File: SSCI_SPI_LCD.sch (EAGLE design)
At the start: 33 parts, among them IC3 74LVC541_RGY, X1 PHA-1X08SG, X2 PHA-1X08SG

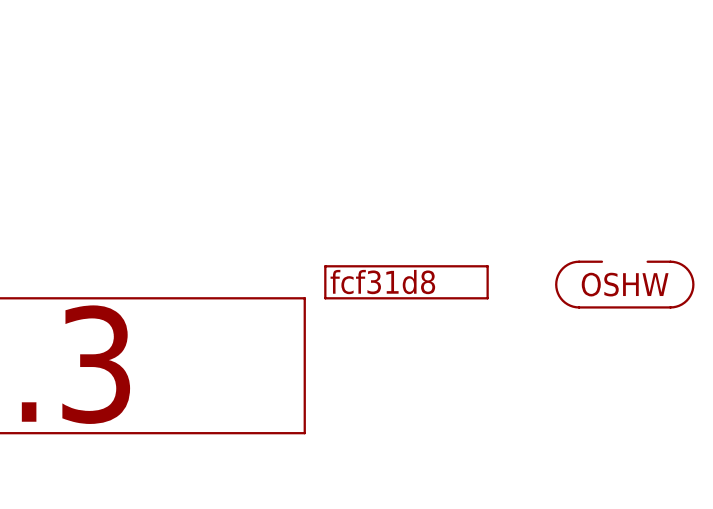
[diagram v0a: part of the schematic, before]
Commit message: update git revision; remove unnecessary tRestrict
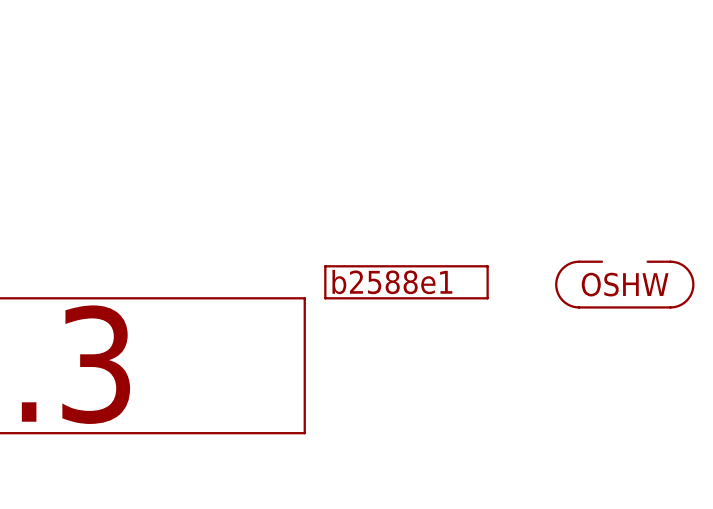
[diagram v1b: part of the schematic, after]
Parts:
- GIT1: value fcf31d8 -> b2588e1
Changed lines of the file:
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@@
 <part name="P3" library="mylib" deviceset="PCB_CORNER" device=""/>
 <part name="P4" library="mylib" deviceset="PCB_CORNER" device=""/>
-<part name="GIT1" library="git-revision" deviceset="GIT-REVISION" device="_1.2" value="fcf31d8"/>
+<part name="GIT1" library="git-revision" deviceset="GIT-REVISION" device="_1.2" value="b2588e1"/>
 <part name="FRAME1" library="frames" deviceset="A4L-LOC" device=""/>
 <part name="ICON1" library="mylib" deviceset="ICON_REVISION" device="_1.7" value="r0.3"/>

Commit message: pin header distance get 200mil narrower
- 1300mil -> 1100mil
- matches with "standard" breadboard
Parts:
- R1: NOT_COMPONENT (none) -> YES
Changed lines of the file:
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@@
 <part name="SUPPLY7" library="mylib" deviceset="GND" device=""/>
 <part name="R2" library="mylib" deviceset="R_US_*" device="_1005" technology="10K"/>
-<part name="R1" library="mylib" deviceset="R_US_*" device="_1005" technology="10K"/>
+<part name="R1" library="mylib" deviceset="R_US_*" device="_1005" technology="10K">
+<attribute name="NOT_COMPONENT" value="YES"/>
+</part>
 <part name="R5" library="mylib" deviceset="R_US_*" device="_1005" technology="10K"/>
 <part name="R3" library="mylib" deviceset="R_US_*" device="_1005" technology="10K"/>
@@
 <instance part="SUPPLY7" gate="GND" x="182.88" y="76.2"/>
 <instance part="R2" gate="G$1" x="83.82" y="160.02"/>
-<instance part="R1" gate="G$1" x="83.82" y="162.56"/>
+<instance part="R1" gate="G$1" x="83.82" y="162.56">
+<attribute name="NOT_COMPONENT" x="83.82" y="162.56" size="1.778" layer="96" display="off"/>
+</instance>
 <instance part="R5" gate="G$1" x="83.82" y="147.32"/>
 <instance part="R3" gate="G$1" x="83.82" y="152.4"/>

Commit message: update library
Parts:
- GIT1: value b2588e1 -> f4c890b
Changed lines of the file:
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@@
 <part name="P3" library="mylib" deviceset="PCB_CORNER" device=""/>
 <part name="P4" library="mylib" deviceset="PCB_CORNER" device=""/>
-<part name="GIT1" library="git-revision" deviceset="GIT-REVISION" device="_1.2" value="b2588e1"/>
+<part name="GIT1" library="git-revision" deviceset="GIT-REVISION" device="_1.2" value="f4c890b"/>
 <part name="FRAME1" library="frames" deviceset="A4L-LOC" device=""/>
 <part name="ICON1" library="mylib" deviceset="ICON_REVISION" device="_1.7" value="r0.3"/>

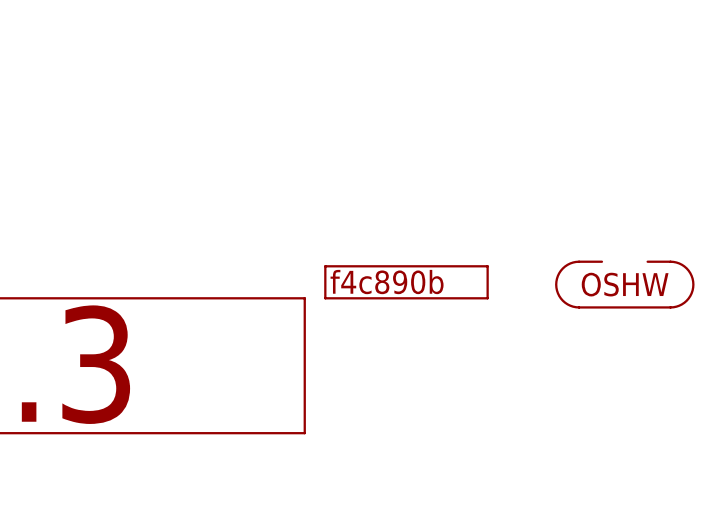
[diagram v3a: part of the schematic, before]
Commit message: outline resized
- no more corner screw holes
- still panelized in 110x100(3x2)
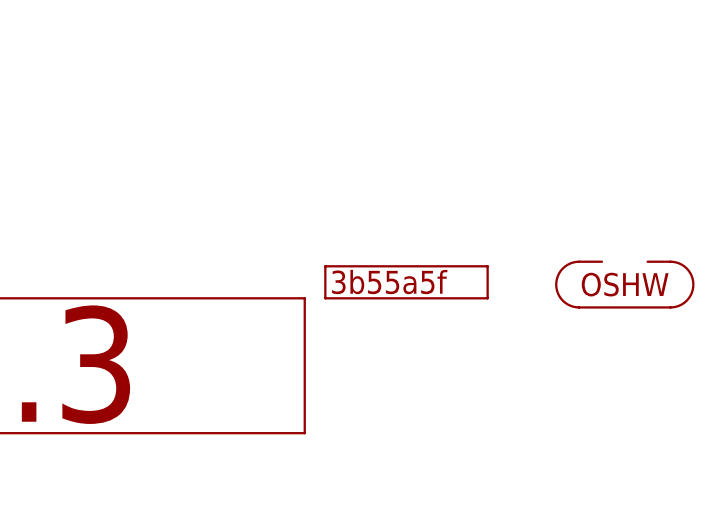
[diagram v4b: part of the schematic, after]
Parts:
- GIT1: value f4c890b -> 3b55a5f
- P1, P2, P3, P4: device mylib:PCB_CORNER -> mylib:PCB_CORNER_NH
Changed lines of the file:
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@@
 <parts>
 <part name="LCD1" library="mylib" deviceset="LCD_GLCD_400X240" device=""/>
-<part name="P1" library="mylib" deviceset="PCB_CORNER" device=""/>
-<part name="P2" library="mylib" deviceset="PCB_CORNER" device=""/>
-<part name="P3" library="mylib" deviceset="PCB_CORNER" device=""/>
-<part name="P4" library="mylib" deviceset="PCB_CORNER" device=""/>
-<part name="GIT1" library="git-revision" deviceset="GIT-REVISION" device="_1.2" value="f4c890b"/>
+<part name="P1" library="mylib" deviceset="PCB_CORNER" device="_NH"/>
+<part name="P2" library="mylib" deviceset="PCB_CORNER" device="_NH"/>
+<part name="P3" library="mylib" deviceset="PCB_CORNER" device="_NH"/>
+<part name="P4" library="mylib" deviceset="PCB_CORNER" device="_NH"/>
+<part name="GIT1" library="git-revision" deviceset="GIT-REVISION" device="_1.2" value="3b55a5f"/>
 <part name="FRAME1" library="frames" deviceset="A4L-LOC" device=""/>
 <part name="ICON1" library="mylib" deviceset="ICON_REVISION" device="_1.7" value="r0.3"/>

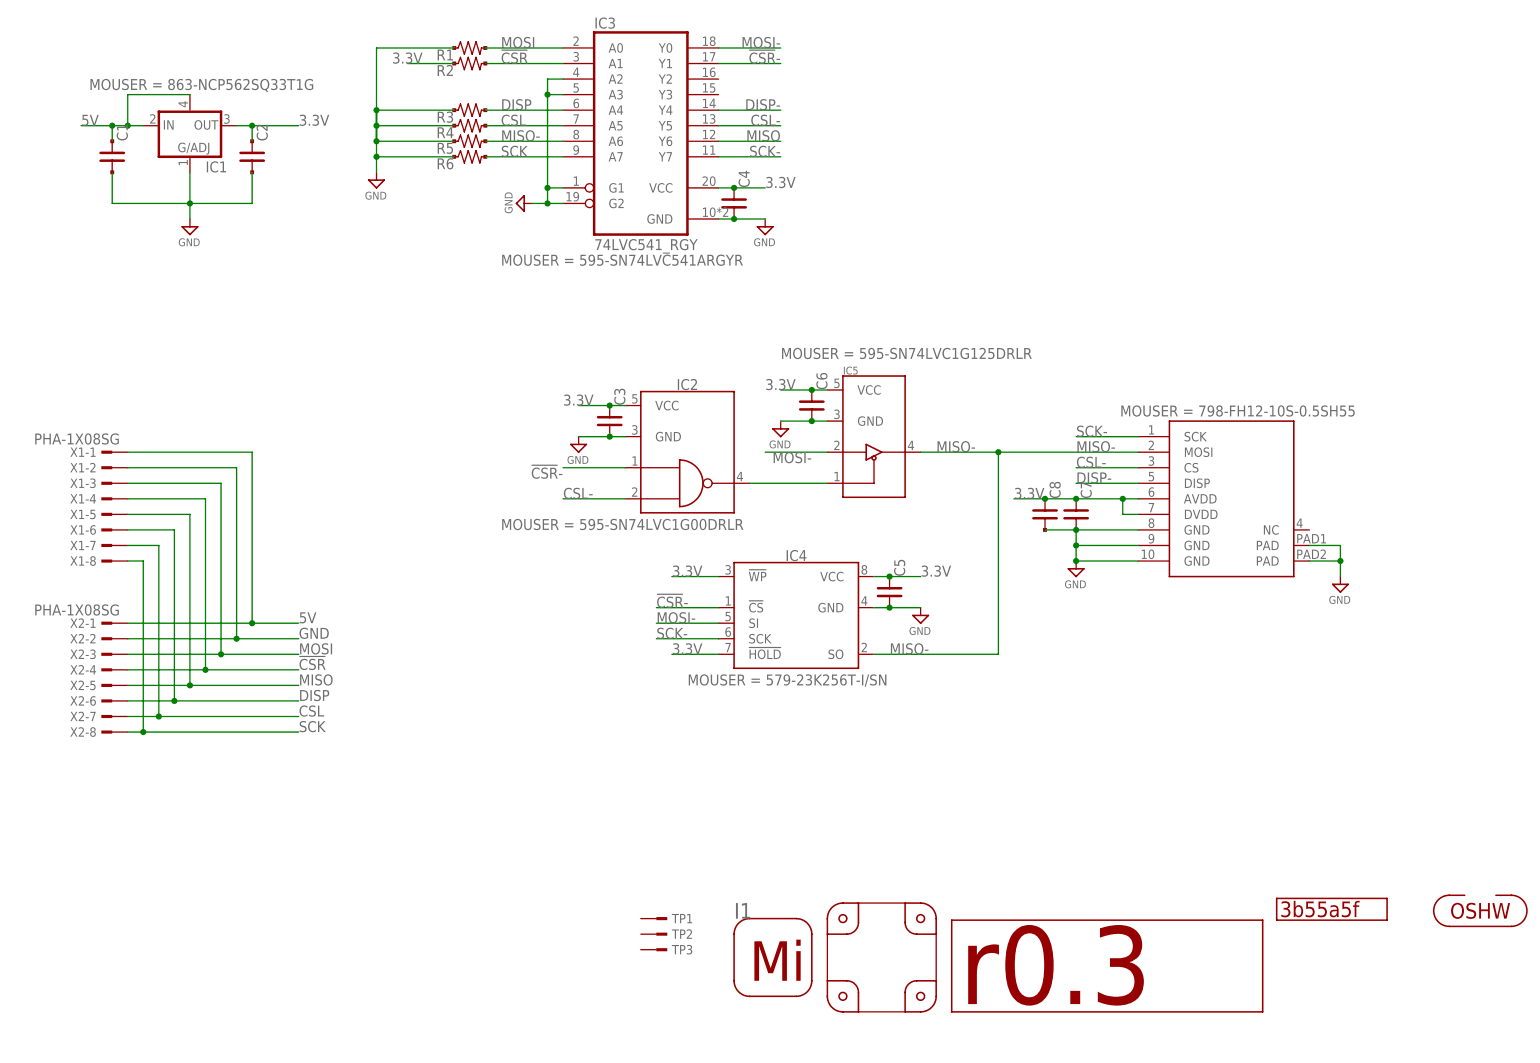
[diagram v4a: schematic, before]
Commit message: R3 connected to 3.3V (to pull up DISP pin)
- left-top corner(at LCD top view) has key-hole
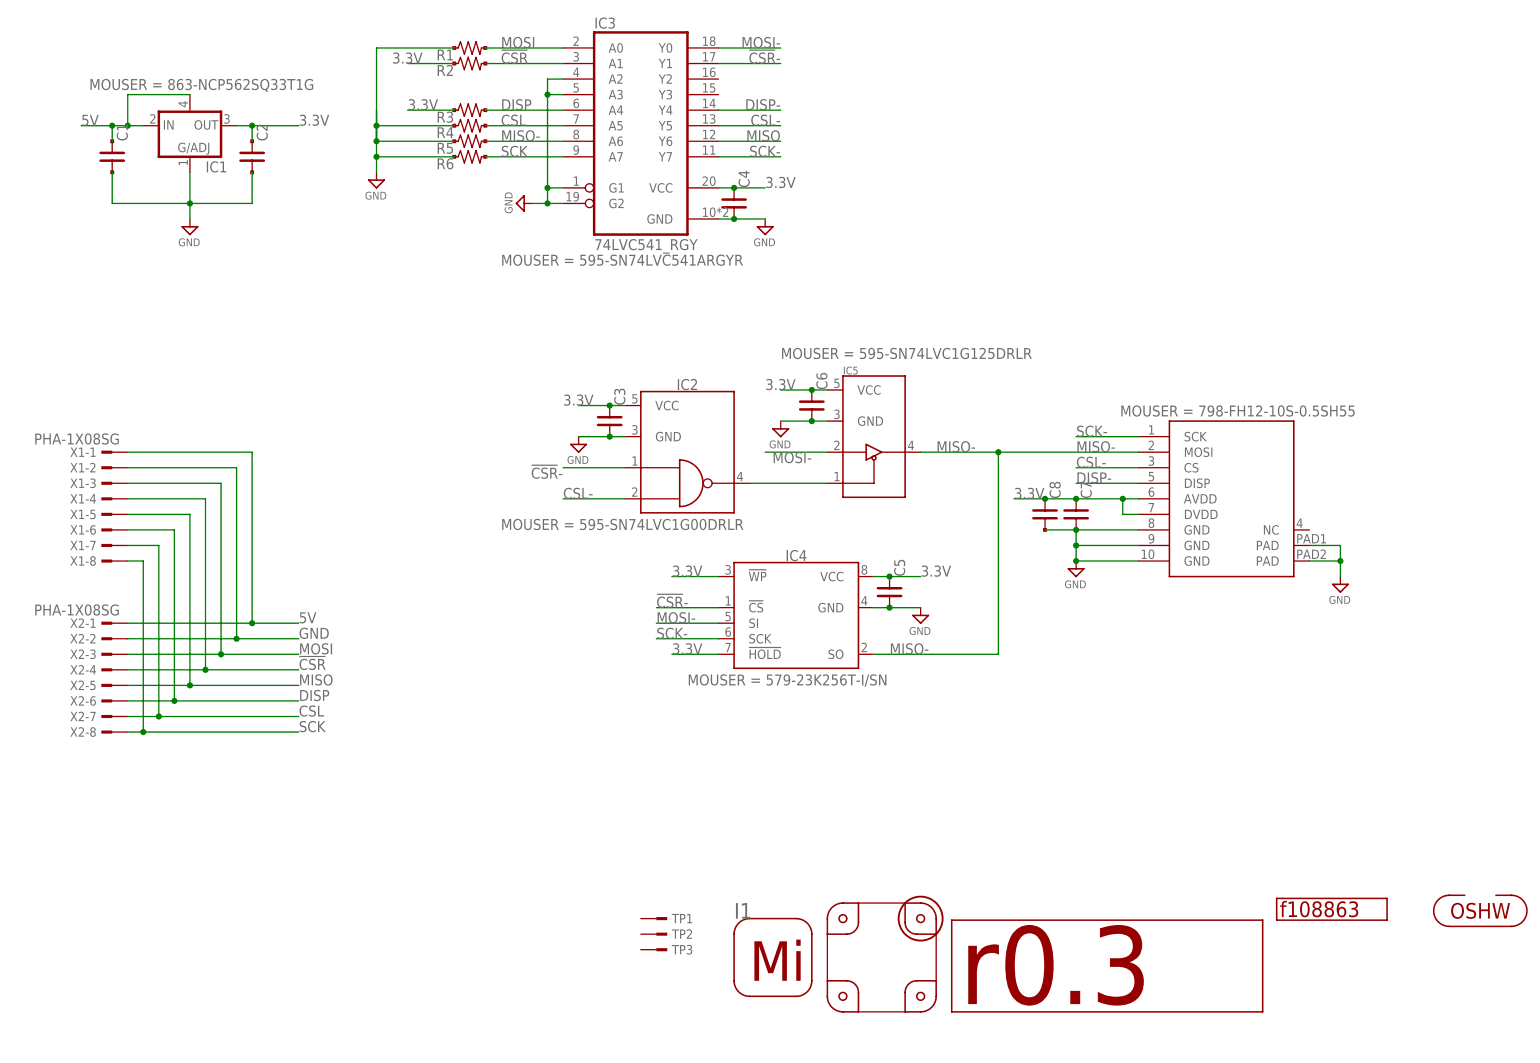
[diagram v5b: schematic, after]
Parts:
- GIT1: value 3b55a5f -> f108863
- P2: device mylib:PCB_CORNER_NH -> mylib:PCB_CORNER
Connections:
- net 3.3V: now also R3.1
- net GND: no longer R3.1
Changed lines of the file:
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@@
 <part name="LCD1" library="mylib" deviceset="LCD_GLCD_400X240" device=""/>
 <part name="P1" library="mylib" deviceset="PCB_CORNER" device="_NH"/>
-<part name="P2" library="mylib" deviceset="PCB_CORNER" device="_NH"/>
+<part name="P2" library="mylib" deviceset="PCB_CORNER" device=""/>
 <part name="P3" library="mylib" deviceset="PCB_CORNER" device="_NH"/>
 <part name="P4" library="mylib" deviceset="PCB_CORNER" device="_NH"/>
-<part name="GIT1" library="git-revision" deviceset="GIT-REVISION" device="_1.2" value="3b55a5f"/>
+<part name="GIT1" library="git-revision" deviceset="GIT-REVISION" device="_1.2" value="f108863"/>
 <part name="FRAME1" library="frames" deviceset="A4L-LOC" device=""/>
 <part name="ICON1" library="mylib" deviceset="ICON_REVISION" device="_1.7" value="r0.3"/>
@@
 <wire x1="142.24" y1="17.78" x2="142.24" y2="10.16" width="0.1524" layer="94"/>
 <wire x1="147.32" y1="5.08" x2="154.94" y2="5.08" width="0.1524" layer="94"/>
+<circle x="157.48" y="20.32" radius="3.5921" width="0.3048" layer="94"/>
 </plain>
 <instances>
@@
 <attribute name="MOUSER" x="228.6" y="104.14" size="1.778" layer="96" rot="R180" display="both"/>
 </instance>
-<instance part="P1" gate="G$1" x="154.94" y="17.78" rot="R90"/>
-<instance part="P2" gate="G$1" x="147.32" y="17.78" rot="R180"/>
+<instance part="P1" gate="G$1" x="147.32" y="17.78" rot="R180"/>
+<instance part="P2" gate="G$1" x="154.94" y="17.78" rot="R90"/>
 <instance part="P3" gate="G$1" x="147.32" y="10.16" rot="R270"/>
 <instance part="P4" gate="G$1" x="154.94" y="10.16"/>
@@
 <pinref part="SUPPLY8" gate="GND" pin="GND"/>
 <pinref part="R1" gate="G$1" pin="1"/>
-<wire x1="68.58" y1="147.32" x2="68.58" y2="152.4" width="0.1524" layer="91"/>
+<wire x1="68.58" y1="147.32" x2="68.58" y2="149.86" width="0.1524" layer="91"/>
 <wire x1="68.58" y1="152.4" x2="68.58" y2="149.86" width="0.1524" layer="91"/>
 <wire x1="68.58" y1="149.86" x2="68.58" y2="147.32" width="0.1524" layer="91"/>
@@
 <wire x1="81.28" y1="147.32" x2="68.58" y2="147.32" width="0.1524" layer="91"/>
 <junction x="68.58" y="147.32"/>
-<pinref part="R3" gate="G$1" pin="1"/>
-<wire x1="81.28" y1="152.4" x2="68.58" y2="152.4" width="0.1524" layer="91"/>
-<junction x="68.58" y="152.4"/>
 <pinref part="R4" gate="G$1" pin="1"/>
 <wire x1="81.28" y1="149.86" x2="68.58" y2="149.86" width="0.1524" layer="91"/>
@@
 <label x="71.12" y="160.02" size="1.778" layer="95"/>
 </segment>
-</net>
+<segment>
+<wire x1="73.66" y1="152.4" x2="81.28" y2="152.4" width="0.1524" layer="91"/>
+<label x="73.66" y="152.4" size="1.778" layer="95"/>
+<pinref part="R3" gate="G$1" pin="1"/>
+</segment>
+</net>

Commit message: keyhole replaced by milling
X2 note is tPlace layer
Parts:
- P2: device mylib:PCB_CORNER -> mylib:PCB_CORNER_NH
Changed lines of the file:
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@@
 <part name="LCD1" library="mylib" deviceset="LCD_GLCD_400X240" device=""/>
 <part name="P1" library="mylib" deviceset="PCB_CORNER" device="_NH"/>
-<part name="P2" library="mylib" deviceset="PCB_CORNER" device=""/>
+<part name="P2" library="mylib" deviceset="PCB_CORNER" device="_NH"/>
 <part name="P3" library="mylib" deviceset="PCB_CORNER" device="_NH"/>
 <part name="P4" library="mylib" deviceset="PCB_CORNER" device="_NH"/>

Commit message: 8c37b00 panelized
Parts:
- GIT1: value f108863 -> 8c37b00
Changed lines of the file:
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@@
 <part name="P3" library="mylib" deviceset="PCB_CORNER" device="_NH"/>
 <part name="P4" library="mylib" deviceset="PCB_CORNER" device="_NH"/>
-<part name="GIT1" library="git-revision" deviceset="GIT-REVISION" device="_1.2" value="f108863"/>
+<part name="GIT1" library="git-revision" deviceset="GIT-REVISION" device="_1.2" value="8c37b00"/>
 <part name="FRAME1" library="frames" deviceset="A4L-LOC" device=""/>
 <part name="ICON1" library="mylib" deviceset="ICON_REVISION" device="_1.7" value="r0.3"/>
